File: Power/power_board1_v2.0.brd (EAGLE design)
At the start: 106.7 x 57.1 mm, 58 parts, among them J0_PLOAD_CONN 172648-0102, J1_B3_CONN 105313-1102, J2_LORA_CONN 105313-1102, J3_SPOT_CONN 105313-1102, J4_SSSBOARD_CONN 172648-0102, Q1 FQD11P06TM

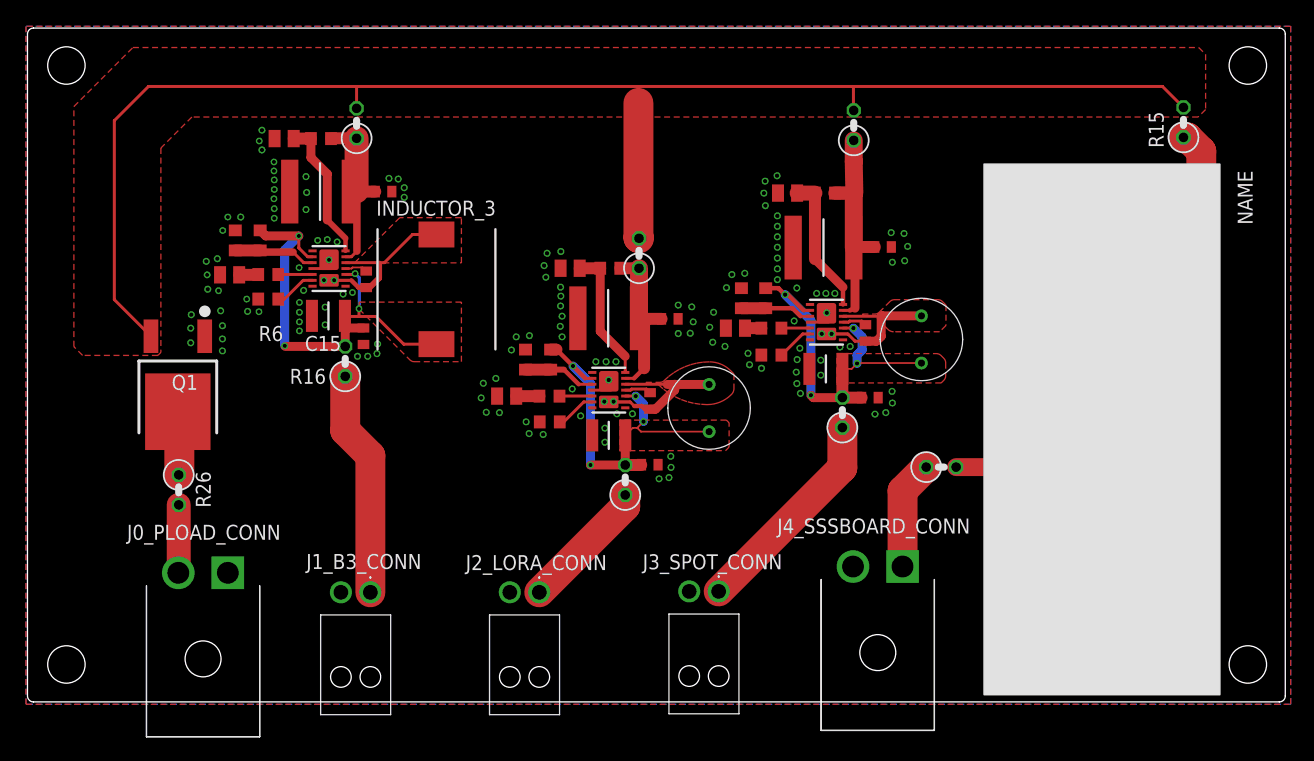
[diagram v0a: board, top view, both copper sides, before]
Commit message: Redesigned layout to fit in AUV. Changed 18V and 24V to mini and micro (also vertical), tucked connectors into board, all wrapped up
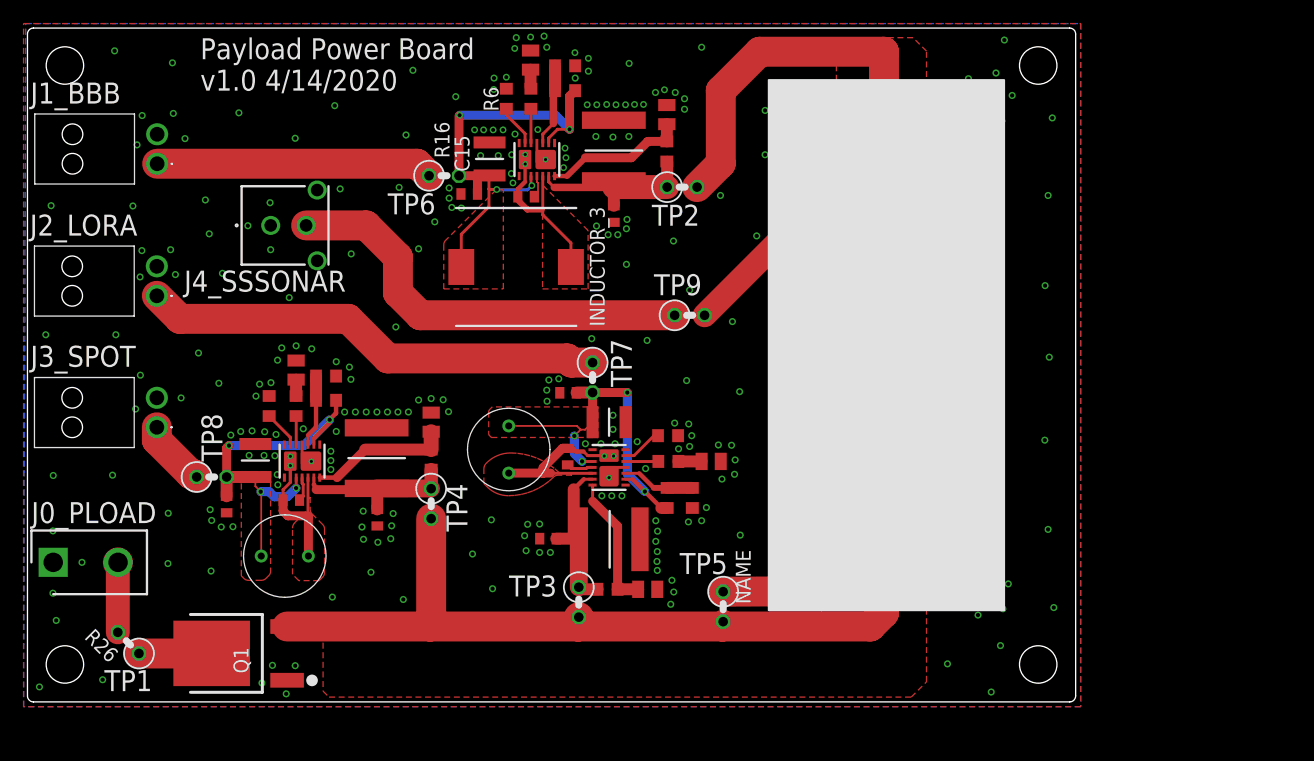
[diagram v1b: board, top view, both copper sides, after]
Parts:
- J0_PLOAD_CONN: value 172648-0102 -> 0039281023; device 172648-0102:1726480102 -> 0039281023:SHDR2W145P0X550_1X2_960X540X13
- J4_SSSBOARD_CONN: value 172648-0102 -> 43045-0212; device 172648-0102:1726480102 -> 43045-0212:0430450212
- moved J4_SSSBOARD_CONN 63.1 mm to (18.2, 40.4), turned to 270 degrees
- moved R15 56.7 mm to (59.0, 8.08), turned to 270 degrees
- moved L4 55.8 mm to (23.8, 12.4), turned to 270 degrees
- moved C6 55.3 mm to (16.9, 16.7), turned to 270 degrees
- moved R21 53.8 mm to (15.6, 19.1), turned to 0 degrees
- moved C4 50.7 mm to (22.4, 17.1), turned to 180 degrees
- moved J3_SPOT_CONN 49.6 mm to (11.0, 23.3), turned to 270 degrees
- moved C12 49.0 mm to (19.3, 20.5), turned to 90 degrees
- moved C9 48.7 mm to (29.7, 15.6), turned to 270 degrees
- moved R14 48.1 mm to (34.2, 16.8), turned to 270 degrees
- moved SPOT_VOLT_REG 46.0 mm to (23.3, 20.4), turned to 180 degrees
- moved R10 42.8 mm to (20.5, 25.1), turned to 270 degrees
- moved C35 41.9 mm to (29.6, 20.7), turned to 90 degrees
- moved J2_LORA_CONN 41.0 mm to (11.0, 34.4), turned to 270 degrees
- moved R11 40.8 mm to (22.8, 25.1), turned to 270 degrees
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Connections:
- net GND: now also J4_SSSBOARD_CONN.1; no longer J4_SSSBOARD_CONN.2
- net V_SSS1: now also J4_SSSBOARD_CONN.2; no longer J4_SSSBOARD_CONN.1
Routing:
- net V_LORA1: track 11.3 -> 39.3 mm
- net V_SSS1: track 9.26 -> 36.2 mm
- net V_SPOT1: track 18.2 -> 5.76 mm
- net V_SSS: track 28.1 -> 21.3 mm
- net VIN_SPOT: track 18.8 -> 14.3 mm
- net V_PLOAD: track 129.0 -> 133.3 mm
- net V_B31: track 19.2 -> 23.5 mm
- net V_PLOAD0: track 5.46 -> 7.05 mm
- net GND: track 0.00 -> 1.06 mm, vias 138 -> 260
- net SW_LORA: track 14.8 -> 15.6 mm
- net VIN_XL6009: track 4.70 -> 5.45 mm
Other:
- board size 106.7 x 57.1 mm -> 88.9 x 57.1 mm
- board text added: "J0_PLOAD"
- board text added: "J1_BBB"
- board text added: "J2_LORA"
- board text added: "J3_SPOT"
- board text added: "J4_SSSONAR"
- board text added: "Payload Power Board v1.0 4/14/2020"
- board text added: "TP1"
- board text added: "TP2"
- board text added: "TP3"
- board text added: "TP4"
- board text added: "TP5"
- board text added: "TP6"
- board text added: "TP7"
- board text added: "TP8"
- board text added: "TP9"

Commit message: Forgot to add names to components (helpful for assembly)
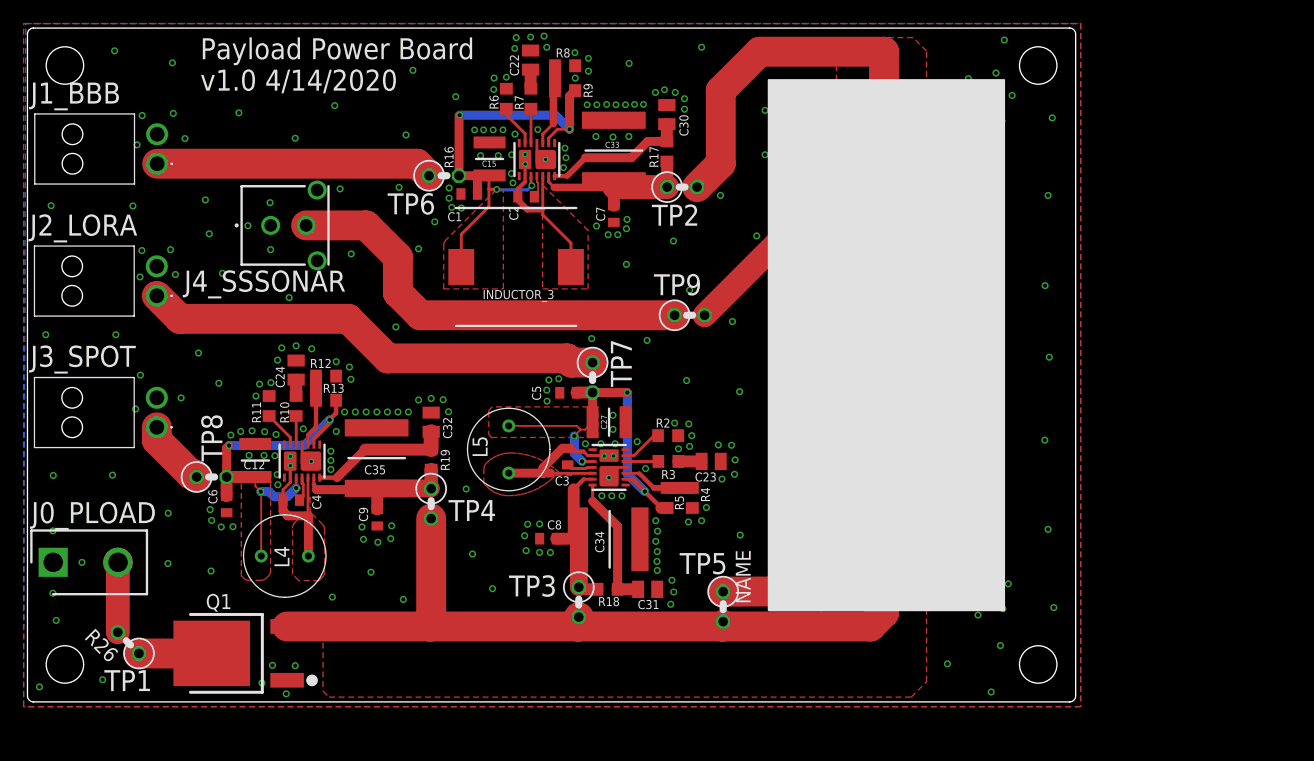
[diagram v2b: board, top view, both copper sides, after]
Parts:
- XL6009_BOOST_CONV_DAUGHTERBOARD: value CP8-ADJ -> XL6009
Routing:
- net GND: vias 260 -> 258

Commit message: Boards being made at OSHPark were wrt these files
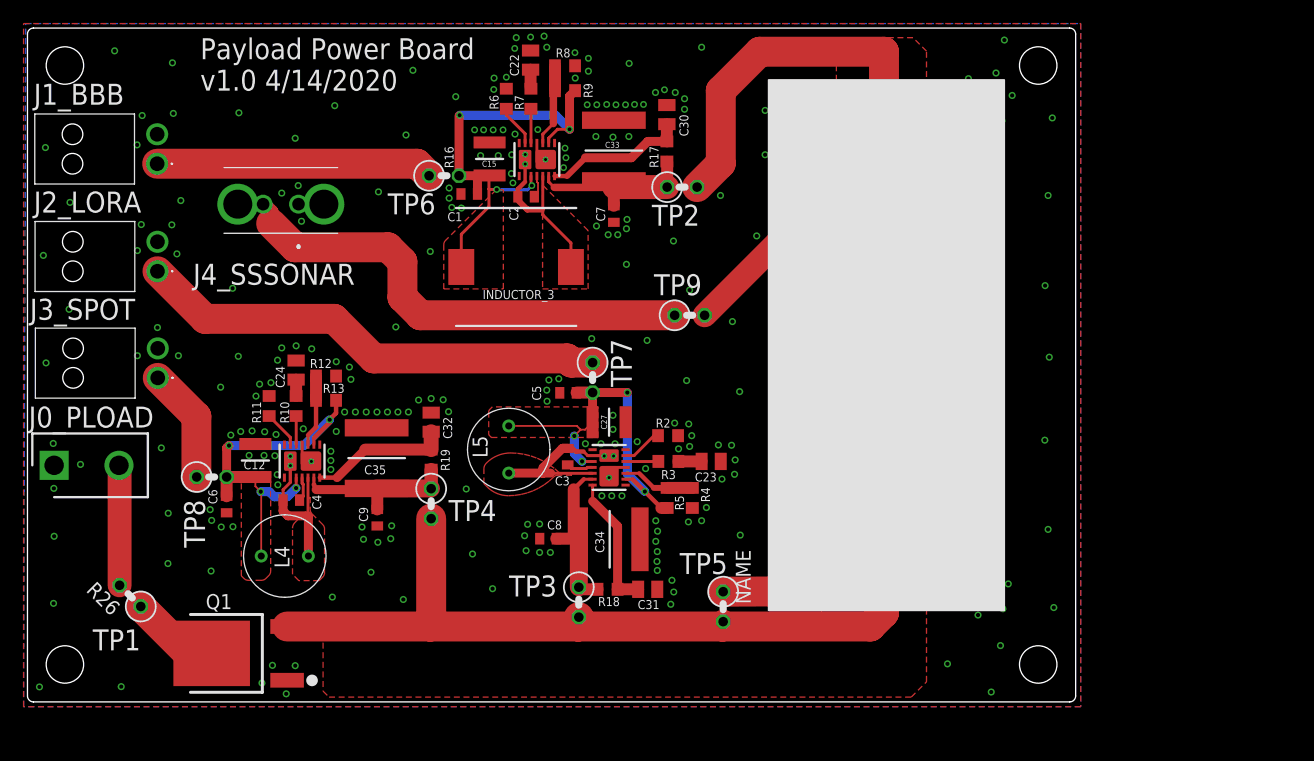
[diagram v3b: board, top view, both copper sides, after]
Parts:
- J4_SSSBOARD_CONN: value 43045-0212 -> 43650-0218; device 43045-0212:0430450212 -> 43650-0218:436500218
- moved J0_PLOAD_CONN 8.23 mm to (2.26, 20.1)
- moved J4_SSSBOARD_CONN 5.15 mm to (23.0, 42.2), turned to 0 degrees
- moved J3_SPOT_CONN 4.19 mm to (11.0, 27.5)
- moved R26 3.99 mm to (8.71, 8.99)
- moved J2_LORA_CONN 2.08 mm to (11.0, 36.5)
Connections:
- net VIN_XL6009 renamed VIN_SSS
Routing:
- net V_SSS1: track 36.2 -> 41.1 mm
- net V_PLOAD00: track 5.94 -> 10.2 mm
- net V_SPOT1: track 5.76 -> 9.78 mm
- net V_LORA1: track 39.3 -> 40.1 mm
- net V_PLOAD0: track 7.05 -> 7.66 mm
- net GND: vias 258 -> 253
